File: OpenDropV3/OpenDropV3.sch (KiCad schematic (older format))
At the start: 257 parts, among them J1 USB_C_Receptacle, J2 Conn_02x05_Odd_Even, P1 CONN_01X01, P10 CONN_01X01, P11 CONN_01X01, P12 CONN_01X01, P13 ScrewPad1, P14 ScrewPad2, P15 ScrewPad3, P16 ScrewPad4, P2 ScrewPad4, P3 CONN_01X01, P4 CONN_PSEUDO_AC, P7 CONN_01X01, P8 CONN_01X01, P9 CONN_01X01, SW1 SW_PUSH, SW2 SW_PUSH, SW3 SW_PUSH, SW5 SPST, T1 TK560P60Y, U1 MAX1771ESA, U10 AQY210EH, U11 AQY210EH, U12 AQY210EH, U13 AQY210EH, U14 TLV1117-33, U15 MCP41010, U16 74xx14, U2 HV507, U3 PAM8301, U4 HV507, U5 SAMD21G18B-A changed from SAM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, U6 MCP6002, U7 HCPL0534, U8 HCPL0534, U9 HCPL0534, Y1 32.765

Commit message: Add USB C pulldowns
Fixes #12
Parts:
- added R14, R23: 5.1k, Resistors_SMD:R_0805, symbol R
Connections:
- net GND: now also R14.1, R23.1
- net at J1.A5 (CC1): now also R23.2
- net at J1.B5 (CC2): now also R14.2
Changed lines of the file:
@@
 LIBS:contrib
 LIBS:valves
-LIBS:GaudiLabsPartsLibrary
 LIBS:OpenDropV3-cache
 EELAYER 25 0
@@
 	2750 3100 3800 3100
 Wire Wire Line
-	7800 3250 7800 3550
+	7800 3550 7800 3250
 Wire Wire Line
 	6200 3700 6200 3550
@@
 	1    0    0    -1
 $EndComp
+$Comp
+L R R23
+U 1 1 5B454B39
+P 22300 12250
+F 0 "R23" H 22200 12100 50  0000 C CNN
+F 1 "5.1k" V 22400 12250 50  0000 C CNN
+F 2 "Resistors_SMD:R_0805" V 22230 12250 30  0001 C CNN
+F 3 "" H 22300 12250 30  0000 C CNN
+	1    22300 12250
+	-1   0    0    1
+$EndComp
+$Comp
+L R R14
+U 1 1 5B4568FE
+P 22050 12250
+F 0 "R14" H 21950 12100 50  0000 C CNN
+F 1 "5.1k" V 22150 12250 50  0000 C CNN
+F 2 "Resistors_SMD:R_0805" V 21980 12250 30  0001 C CNN
+F 3 "" H 22050 12250 30  0000 C CNN
+	1    22050 12250
+	-1   0    0    1
+$EndComp
+Wire Wire Line
+	21350 12100 22050 12100
+Wire Wire Line
+	21350 12000 22300 12000
+Wire Wire Line
+	22300 12000 22300 12100
+$Comp
+L GND #PWR059
+U 1 1 5B45D041
+P 22300 12400
+F 0 "#PWR059" H 22300 12150 50  0001 C CNN
+F 1 "GND" H 22300 12250 50  0000 C CNN
+F 2 "" H 22300 12400 60  0000 C CNN
+F 3 "" H 22300 12400 60  0000 C CNN
+	1    22300 12400
+	1    0    0    -1
+$EndComp
+Wire Wire Line
+	22050 12400 22300 12400
 $EndSCHEMATC

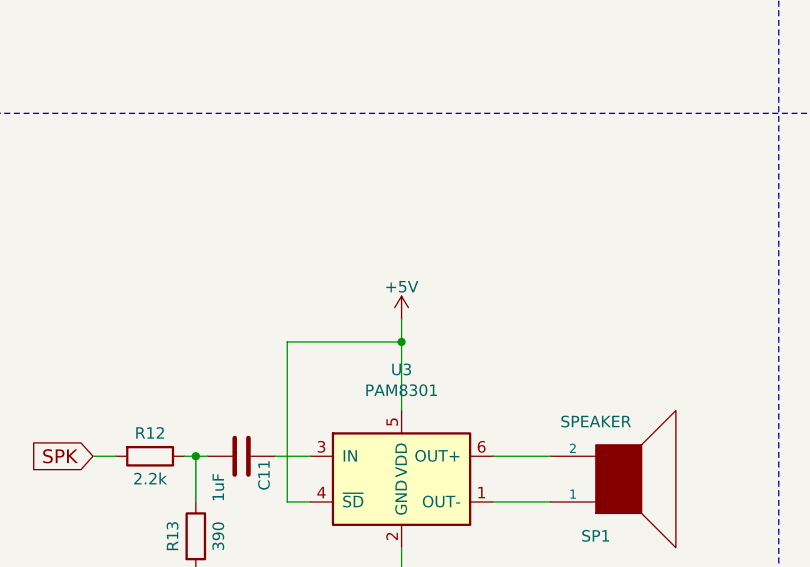
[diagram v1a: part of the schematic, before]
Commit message: Connect speaker driver to 3.3V (instead of 5V)
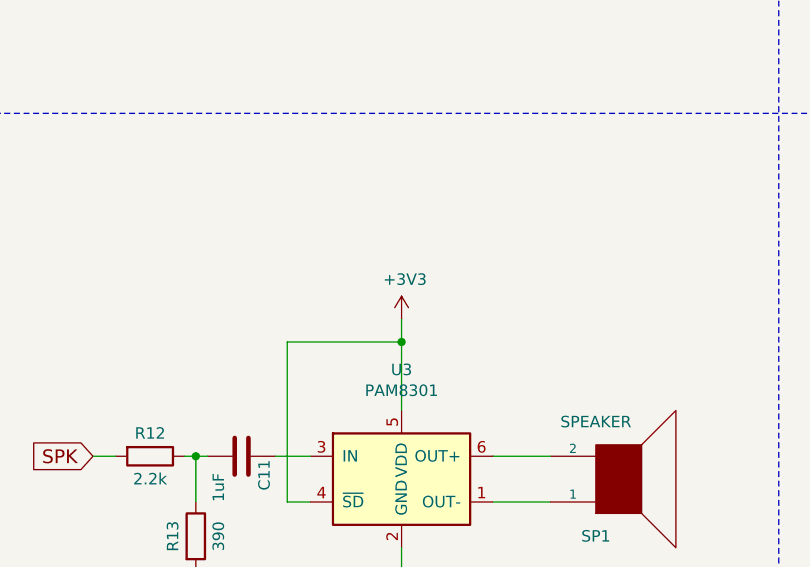
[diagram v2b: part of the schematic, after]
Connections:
- net +3V3: now also U3.4 (~SD), U3.5 (VDD)
- net +5V: no longer U3.4 (~SD), U3.5 (VDD)
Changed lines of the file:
@@
-$EndComp
-$Comp
-L +3V3 #PWR037
-U 1 1 59D4EB17
-P 16550 10800
-F 0 "#PWR037" H 16550 10650 50  0001 C CNN
-F 1 "+3V3" H 16565 10973 50  0000 C CNN
-F 2 "" H 16550 10800 50  0001 C CNN
-F 3 "" H 16550 10800 50  0001 C CNN
-	1    16550 10800
-	1    0    0    -1
 $EndComp
 $Comp
@@
 $EndComp
 $Comp
-L GND #PWR038
+L GND #PWR037
 U 1 1 59D661A5
 P 14450 14800
-F 0 "#PWR038" H 14450 14550 50  0001 C CNN
+F 0 "#PWR037" H 14450 14550 50  0001 C CNN
 F 1 "GND" H 14450 14650 50  0000 C CNN
 F 2 "" H 14450 14800 60  0000 C CNN
@@
 $EndComp
 $Comp
-L +3V3 #PWR039
+L +3V3 #PWR038
 U 1 1 59CD8BFE
 P 13100 5100
-F 0 "#PWR039" H 13100 4950 50  0001 C CNN
+F 0 "#PWR038" H 13100 4950 50  0001 C CNN
 F 1 "+3V3" H 13115 5273 50  0000 C CNN
 F 2 "" H 13100 5100 50  0001 C CNN
@@
 $EndComp
 $Comp
-L GND #PWR040
+L GND #PWR039
 U 1 1 59CD97E2
 P 13100 5700
-F 0 "#PWR040" H 13100 5450 50  0001 C CNN
+F 0 "#PWR039" H 13100 5450 50  0001 C CNN
 F 1 "GND" H 13100 5550 50  0000 C CNN
 F 2 "" H 13100 5700 60  0000 C CNN
@@
 $EndComp
 $Comp
-L +3V3 #PWR041
+L +3V3 #PWR040
 U 1 1 59CE7BDF
 P 11950 5950
-F 0 "#PWR041" H 11950 5800 50  0001 C CNN
+F 0 "#PWR040" H 11950 5800 50  0001 C CNN
 F 1 "+3V3" H 11965 6123 50  0000 C CNN
 F 2 "" H 11950 5950 50  0001 C CNN
@@
 $EndComp
 $Comp
-L GND #PWR042
+L GND #PWR041
 U 1 1 59CFF82D
 P 13750 11700
-F 0 "#PWR042" H 13750 11450 50  0001 C CNN
+F 0 "#PWR041" H 13750 11450 50  0001 C CNN
 F 1 "GND" H 13750 11550 50  0000 C CNN
 F 2 "" H 13750 11700 60  0000 C CNN
@@
 $EndComp
 $Comp
-L +3V3 #PWR043
+L +3V3 #PWR042
 U 1 1 59E92B25
 P 17700 1850
-F 0 "#PWR043" H 17700 1700 50  0001 C CNN
+F 0 "#PWR042" H 17700 1700 50  0001 C CNN
 F 1 "+3V3" H 17715 2023 50  0000 C CNN
 F 2 "" H 17700 1850 50  0001 C CNN
@@
 $EndComp
 $Comp
-L +3V3 #PWR044
+L +3V3 #PWR043
 U 1 1 59E968E0
 P 18550 1850
-F 0 "#PWR044" H 18550 1700 50  0001 C CNN
+F 0 "#PWR043" H 18550 1700 50  0001 C CNN
 F 1 "+3V3" H 18565 2023 50  0000 C CNN
 F 2 "" H 18550 1850 50  0001 C CNN
@@
 $EndComp
 $Comp
-L +3V3 #PWR045
+L +3V3 #PWR044
 U 1 1 59E97E88
 P 20250 1850
-F 0 "#PWR045" H 20250 1700 50  0001 C CNN
+F 0 "#PWR044" H 20250 1700 50  0001 C CNN
 F 1 "+3V3" H 20265 2023 50  0000 C CNN
 F 2 "" H 20250 1850 50  0001 C CNN
@@
 $EndComp
 $Comp
-L +3V3 #PWR046
+L +3V3 #PWR045
 U 1 1 59E99EAB
 P 15400 2450
-F 0 "#PWR046" H 15400 2300 50  0001 C CNN
+F 0 "#PWR045" H 15400 2300 50  0001 C CNN
 F 1 "+3V3" H 15415 2623 50  0000 C CNN
 F 2 "" H 15400 2450 50  0001 C CNN
@@
 $EndComp
 $Comp
-L +5V #PWR047
-U 1 1 59E0BF80
-P 16600 13350
-F 0 "#PWR047" H 16600 13200 50  0001 C CNN
-F 1 "+5V" H 16600 13490 50  0000 C CNN
-F 2 "" H 16600 13350 60  0000 C CNN
-F 3 "" H 16600 13350 60  0000 C CNN
-	1    16600 13350
-	1    0    0    -1
-$EndComp
-$Comp
 L C C5
 U 1 1 59E0F4C4
@@
 $EndComp
 $Comp
-L GND #PWR048
+L GND #PWR046
 U 1 1 59E0FA6E
 P 13450 11700
-F 0 "#PWR048" H 13450 11450 50  0001 C CNN
+F 0 "#PWR046" H 13450 11450 50  0001 C CNN
 F 1 "GND" H 13450 11550 50  0000 C CNN
 F 2 "" H 13450 11700 60  0000 C CNN
@@
 $EndComp
 $Comp
-L +5V #PWR049
+L +5V #PWR047
 U 1 1 59FE84CA
 P 4050 1850
-F 0 "#PWR049" H 4050 1700 50  0001 C CNN
+F 0 "#PWR047" H 4050 1700 50  0001 C CNN
 F 1 "+5V" H 4050 1990 50  0000 C CNN
 F 2 "" H 4050 1850 60  0000 C CNN
@@
 $EndComp
 $Comp
-L GND #PWR050
+L GND #PWR048
 U 1 1 59FEA75B
 P 3000 4200
-F 0 "#PWR050" H 3000 3950 50  0001 C CNN
+F 0 "#PWR048" H 3000 3950 50  0001 C CNN
 F 1 "GND" H 3000 4050 50  0000 C CNN
 F 2 "" H 3000 4200 60  0000 C CNN
@@
 $EndComp
 $Comp
-L GND #PWR051
+L GND #PWR049
 U 1 1 5A00186C
 P 3000 2700
-F 0 "#PWR051" H 3000 2450 50  0001 C CNN
+F 0 "#PWR049" H 3000 2450 50  0001 C CNN
 F 1 "GND" H 3000 2550 50  0000 C CNN
 F 2 "" H 3000 2700 60  0000 C CNN
@@
 $EndComp
 $Comp
-L GND #PWR052
+L GND #PWR050
 U 1 1 5A0DBA49
 P 13200 11700
-F 0 "#PWR052" H 13200 11450 50  0001 C CNN
+F 0 "#PWR050" H 13200 11450 50  0001 C CNN
 F 1 "GND" H 13200 11550 50  0000 C CNN
 F 2 "" H 13200 11700 60  0000 C CNN
@@
 $EndComp
 $Comp
-L +5V #PWR053
+L +5V #PWR051
 U 1 1 5A0E6981
 P 9800 2350
-F 0 "#PWR053" H 9800 2200 50  0001 C CNN
+F 0 "#PWR051" H 9800 2200 50  0001 C CNN
 F 1 "+5V" H 9800 2490 50  0000 C CNN
 F 2 "" H 9800 2350 60  0000 C CNN
@@
 $EndComp
 $Comp
-L GND #PWR054
+L GND #PWR052
 U 1 1 5A08E614
 P 3300 15450
-F 0 "#PWR054" H 3300 15200 50  0001 C CNN
+F 0 "#PWR052" H 3300 15200 50  0001 C CNN
 F 1 "GND" H 3300 15300 50  0000 C CNN
 F 2 "" H 3300 15450 60  0000 C CNN
@@
 $EndComp
 $Comp
-L +3V3 #PWR055
+L +3V3 #PWR053
 U 1 1 5A0D7EB1
 P 1500 1800
-F 0 "#PWR055" H 1500 1650 50  0001 C CNN
+F 0 "#PWR053" H 1500 1650 50  0001 C CNN
 F 1 "+3V3" H 1515 1973 50  0000 C CNN
 F 2 "" H 1500 1800 50  0001 C CNN
@@
 Connection ~ 21500 11700
 $Comp
-L GND #PWR056
+L GND #PWR054
 U 1 1 5ACB7D35
 P 20650 14550
-F 0 "#PWR056" H 20650 14300 50  0001 C CNN
+F 0 "#PWR054" H 20650 14300 50  0001 C CNN
 F 1 "GND" H 20650 14400 50  0000 C CNN
 F 2 "" H 20650 14550 60  0000 C CNN
@@
 Connection ~ 15700 13950
 $Comp
-L GND #PWR057
+L GND #PWR055
 U 1 1 5ACA682B
 P 15700 14600
-F 0 "#PWR057" H 15700 14350 50  0001 C CNN
+F 0 "#PWR055" H 15700 14350 50  0001 C CNN
 F 1 "GND" H 15700 14450 50  0000 C CNN
 F 2 "" H 15700 14600 60  0000 C CNN
@@
 	3300 14600 3350 14600
 $Comp
-L GND #PWR058
+L GND #PWR056
 U 1 1 5ACB836C
 P 2950 13850
-F 0 "#PWR058" H 2950 13600 50  0001 C CNN
+F 0 "#PWR056" H 2950 13600 50  0001 C CNN
 F 1 "GND" H 2950 13700 50  0000 C CNN
 F 2 "" H 2950 13850 60  0000 C CNN
@@
 	22300 12000 22300 12100
 $Comp
-L GND #PWR059
+L GND #PWR057
 U 1 1 5B45D041
 P 22300 12400
-F 0 "#PWR059" H 22300 12150 50  0001 C CNN
+F 0 "#PWR057" H 22300 12150 50  0001 C CNN
 F 1 "GND" H 22300 12250 50  0000 C CNN
 F 2 "" H 22300 12400 60  0000 C CNN
@@
 Wire Wire Line
 	22050 12400 22300 12400
+$Comp
+L +3V3 #PWR037
+U 1 1 59D4EB17
+P 16600 13350
+F 0 "#PWR037" H 16600 13200 50  0001 C CNN
+F 1 "+3V3" H 16615 13523 50  0000 C CNN
+F 2 "" H 16600 13350 50  0001 C CNN
+F 3 "" H 16600 13350 50  0001 C CNN
+	1    16600 13350
+	1    0    0    -1
+$EndComp
+$Comp
+L +3V3 #PWR?
+U 1 1 5B4D8EBE
+P 16550 10800
+F 0 "#PWR?" H 16550 10650 50  0001 C CNN
+F 1 "+3V3" H 16565 10973 50  0000 C CNN
+F 2 "" H 16550 10800 50  0001 C CNN
+F 3 "" H 16550 10800 50  0001 C CNN
+	1    16550 10800
+	1    0    0    -1
+$EndComp
 $EndSCHEMATC

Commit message: Add MPN field to parts in schematic
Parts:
- C1: MPN (none) -> TPSD107K016R0125
- C10, C8: MPN (none) -> CC0805KKX7R7BB225
- C11, C15, C16, C20, C24, C27, C7, C9: MPN (none) -> CC0805KKX7R7BB105
- C12, C13, C14, C2, C22, C26, C3, C30, C33, C34, C36: MPN (none) -> FS055C104K4Z2A
- C17: MPN (none) -> CL21C010CBANNNC
- C18, C4: MPN (none) -> UUX2G4R7MNL1GS
- C19: MPN (none) -> EEE-FK1V330P
- C21, C5: MPN (none) -> TPSB226K016R0600
- C23, C25: MPN (none) -> C0805C220K5GACTU
- C28, C29: MPN (none) -> 08055A332KAT2A
- C31: MPN (none) -> CL21B224KAFNNNG
- C35, C6: MPN (none) -> C1808V104KBRACTU
- D1: MPN (none) -> ES2FA R3G
- D2, D3: MPN (none) -> 1N4148WS
- J1: MPN (none) -> 12401610E4#2A
- J2: MPN (none) -> 20021121-00010C4LF
- JS1: MPN (none) -> JS5208
- L1: MPN (none) -> SRN1060-101M
- LED1: MPN (none) -> LTST-C190TBKT
- LED2: MPN (none) -> LTST-C190KGKT
- LED3: MPN (none) -> LTST-C190KRKT
- R1: MPN (none) -> RC0805FR-076K8L
- R10, R18, R19, R20, R21, R22, R30, R44, R5: MPN (none) -> RMCF0805FT10K0
- R11: MPN (none) -> AC0805FR-0747KL
- R12, R33, R35, R38, R39, R42, R43: MPN (none) -> RMCF0805FT2K20
- R13, R4, R6, R8: MPN (none) -> RC0805FR-07390RL
- R14, R23: MPN (none) -> RMCF0805FT5K10
- R2: MPN (none) -> ERJ-1TYJ155U
- R3, R9: MPN (none) -> ERJ-6ENF3903V
- R31: MPN (none) -> RMCF0805FT15K0
- R32, R34, R36, R37, R40, R41, R45, R48, R49, R51: MPN (none) -> RMCF0805FT220R
- RSENSE1: MPN (none) -> RCWE1020R100FKEA
- S1: MPN (none) -> SFV30R-1STE1HLF
- SW1, SW2: MPN (none) -> PTS645SM43SMTR92LFS
- SW3: MPN (none) -> KMS231GLFS
- SW5: MPN (none) -> SSA12
- T1: MPN (none) -> TK560P60Y,RQ
- U1: MPN (none) -> MAX1771CSA+T
- U10, U11, U12, U13: MPN (none) -> AQY210EHA
- U14: MPN (none) -> TLV1117LV33DCYR
- U15: MPN (none) -> MCP41010T-I/SN
- U16: MPN (none) -> SN74AC14DR
- U2, U4: MPN (none) -> HV507PG-G
- U3: MPN (none) -> PAM8301AAF
- U5: MPN (none) -> ATSAMD21G18A-AUT
- U6: MPN (none) -> MCP6002T-I/SN
- U7, U8, U9: MPN (none) -> HCPL0534
- Y1: MPN (none) -> LFXTAL009678REEL
